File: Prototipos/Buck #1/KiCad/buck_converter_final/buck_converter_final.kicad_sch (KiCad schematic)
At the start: 31 parts, among them J2 Screw_Terminal_01x02, J3 Screw_Terminal_01x02, K1 SANYOU_SRD_Form_C, Q1 NPN, Q2 IRF9540NPBF, Q3 BC548

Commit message: PCB final, versión preliminar, con testpoints
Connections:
- net PWM_CONTROL: now also J1.15 (S7); no longer J1.9 (S1)
- net RETRO_MICRO: now also J1.17 (S9); no longer J1.11 (S3)
- net UC_RELAY: now also J1.16 (S8); no longer J1.10 (S2)
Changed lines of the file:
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@@
-	(wire
-		(pts
-			(xy 35.56 57.15) (xy 38.1 57.15)
-		)
-		(stroke
-			(width 0)
-			(type default)
-		)
-	)
 	(wire
 		(pts
@@
 	(wire
 		(pts
+			(xy 68.58 52.07) (xy 71.12 52.07)
+		)
+		(stroke
+			(width 0)
+			(type default)
+		)
+	)
+	(wire
+		(pts
 			(xy 259.08 93.98) (xy 261.62 93.98)
 		)
@@
 	(wire
 		(pts
-			(xy 35.56 54.61) (xy 38.1 54.61)
-		)
-		(stroke
-			(width 0)
-			(type default)
-		)
-	)
-	(wire
-		(pts
 			(xy 158.75 101.6) (xy 166.37 101.6)
 		)
@@
 	(wire
 		(pts
-			(xy 35.56 52.07) (xy 38.1 52.07)
-		)
-		(stroke
-			(width 0)
-			(type default)
-		)
-	)
-	(wire
-		(pts
 			(xy 158.75 97.79) (xy 158.75 101.6)
 		)
@@
 	(wire
 		(pts
+			(xy 35.56 69.85) (xy 38.1 69.85)
+		)
+		(stroke
+			(width 0)
+			(type default)
+		)
+	)
+	(wire
+		(pts
 			(xy 58.42 87.63) (xy 58.42 83.82)
 		)
@@
 		(pts
 			(xy 210.82 91.44) (xy 210.82 96.52)
+		)
+		(stroke
+			(width 0)
+			(type default)
+		)
+	)
+	(wire
+		(pts
+			(xy 35.56 67.31) (xy 38.1 67.31)
 		)
 		(stroke
@@
 	(global_label "RETRO_MICRO"
 		(shape input)
-		(at 35.56 57.15 180)
-		(fields_autoplaced yes)
-		(effects
-			(font
-				(size 1.27 1.27)
-			)
-			(justify right)
-		)
-		(property "Intersheetrefs" "${INTERSHEET_REFS}"
-			(at 19.6934 57.15 0)
-			(effects
-				(font
-					(size 1.27 1.27)
-				)
-				(justify right)
+		(at 71.12 52.07 0)
+		(fields_autoplaced yes)
+		(effects
+			(font
+				(size 1.27 1.27)
+			)
+			(justify left)
+		)
+		(property "Intersheetrefs" "${INTERSHEET_REFS}"
+			(at 86.9866 52.07 0)
+			(effects
+				(font
+					(size 1.27 1.27)
+				)
+				(justify left)
 				(hide yes)
 			)
@@
 	(global_label "PWM_CONTROL"
 		(shape output)
-		(at 35.56 52.07 180)
-		(fields_autoplaced yes)
-		(effects
-			(font
-				(size 1.27 1.27)
-			)
-			(justify right)
-		)
-		(property "Intersheetrefs" "${INTERSHEET_REFS}"
-			(at 18.9072 52.07 0)
+		(at 35.56 67.31 180)
+		(fields_autoplaced yes)
+		(effects
+			(font
+				(size 1.27 1.27)
+			)
+			(justify right)
+		)
+		(property "Intersheetrefs" "${INTERSHEET_REFS}"
+			(at 18.9072 67.31 0)
 			(effects
 				(font
@@
 	(global_label "UC_RELAY"
 		(shape output)
-		(at 35.56 54.61 180)
-		(fields_autoplaced yes)
-		(effects
-			(font
-				(size 1.27 1.27)
-			)
-			(justify right)
-		)
-		(property "Intersheetrefs" "${INTERSHEET_REFS}"
-			(at 23.3824 54.61 0)
-			(effects
-				(font
+		(at 35.56 69.85 180)
+		(fields_autoplaced yes)
+		(effects
+			(font
+				(size 1.27 1.27)
+			)
+			(justify right)
+		)
+		(property "Intersheetrefs" "${INTERSHEET_REFS}"
+			(at 23.3824 69.85 0)
+			(effects
+				(font

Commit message: Avances PCB
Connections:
- no-connect marks 0 -> 1
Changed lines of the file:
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@@
 		(color 0 0 0 0)
+	)
+	(no_connect
+		(at 44.45 120.65)
 	)
 	(wire

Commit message: PCB Buck versión 1.0 finalizada
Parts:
- added TP1: DRAIN, TestPoint:TestPoint_Loop_D1.80mm_Drill1.0mm_Beaded, symbol Connector:TestPoint
- added TP2: GATE, TestPoint:TestPoint_Loop_D1.80mm_Drill1.0mm_Beaded, symbol Connector:TestPoint
- added TP3: LOAD_1, TestPoint:TestPoint_Loop_D1.80mm_Drill1.0mm_Beaded, symbol Connector:TestPoint
- added TP4: LOAD_2, TestPoint:TestPoint_Loop_D1.80mm_Drill1.0mm_Beaded, symbol Connector:TestPoint
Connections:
- net GATE: now also TP2.1
- net INDUCTIVE_LOAD: now also TP4.1
- net RESISTIVE_LOAD: now also TP3.1
- net at C3.2, D2.2 (A), D3.1 (K)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: now also TP1.1
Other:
- moved on the sheet: J3

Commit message: Corrección footprint diodo
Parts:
- D3: footprint Diode_THT:D_DO-15_P12.70mm_Horizontal -> Diode_THT:D_DO-201AD_P12.70mm_Horizontal
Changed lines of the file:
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@@
 			)
 		)
-		(property "Footprint" "Diode_THT:D_DO-15_P12.70mm_Horizontal"
+		(property "Footprint" "Diode_THT:D_DO-201AD_P12.70mm_Horizontal"
 			(at 147.32 63.5 90)
 			(effects

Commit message: Corrección nomenclatura, lista de componentes
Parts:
- R10: value 2k2 -> 2.2k
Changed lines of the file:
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@@
 			)
 		)
-		(property "Value" "2k2"
+		(property "Value" "2.2k"
 			(at 172.466 64.516 0)
 			(effects

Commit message: Avances en medición de corriente
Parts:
- added C7, C8: 0.1uF, Capacitor_SMD:C_0805_2012Metric_Pad1.18x1.45mm_HandSolder, symbol Device:C_Small
- added R14, R15: 0.01, Resistor_SMD:R_0805_2012Metric_Pad1.20x1.40mm_HandSolder, symbol Device:R_Small
- added TP5: INDUCOR_CURRENT, TestPoint:TestPoint_Loop_D1.80mm_Drill1.0mm_Beaded, symbol Connector:TestPoint
- added TP6: CAPACITOR_CURRENT, TestPoint:TestPoint_Loop_D1.80mm_Drill1.0mm_Beaded, symbol Connector:TestPoint
- added U1, U2: INA199xxDCK, Package_TO_SOT_SMD:SOT-363_SC-70-6, symbol Amplifier_Current:INA199xxDCK
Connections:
- net 12V: now also C7.1, C8.1, U1.3 (V+), U2.3 (V+)
- net PGND: now also C7.2, R15.1, U1.1 (REF), U1.2 (GND), U2.5 (-); no longer C5.2
- net at C5.1, K1.1, R9.1: now also R14.2, U1.5 (-); no longer L1.2
- new net: TP5.1, U1.6
- new net: C8.2, U2.2 (GND)
- new net: C5.2, R15.2, U2.4 (+)
- new net: TP6.1, U2.6
- new net: L1.2, R14.1, U1.4 (+)
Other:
- moved on the sheet: C2, C5, C6, D1, D4, K1, L1, Q1, Q3, R1, R10, R11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

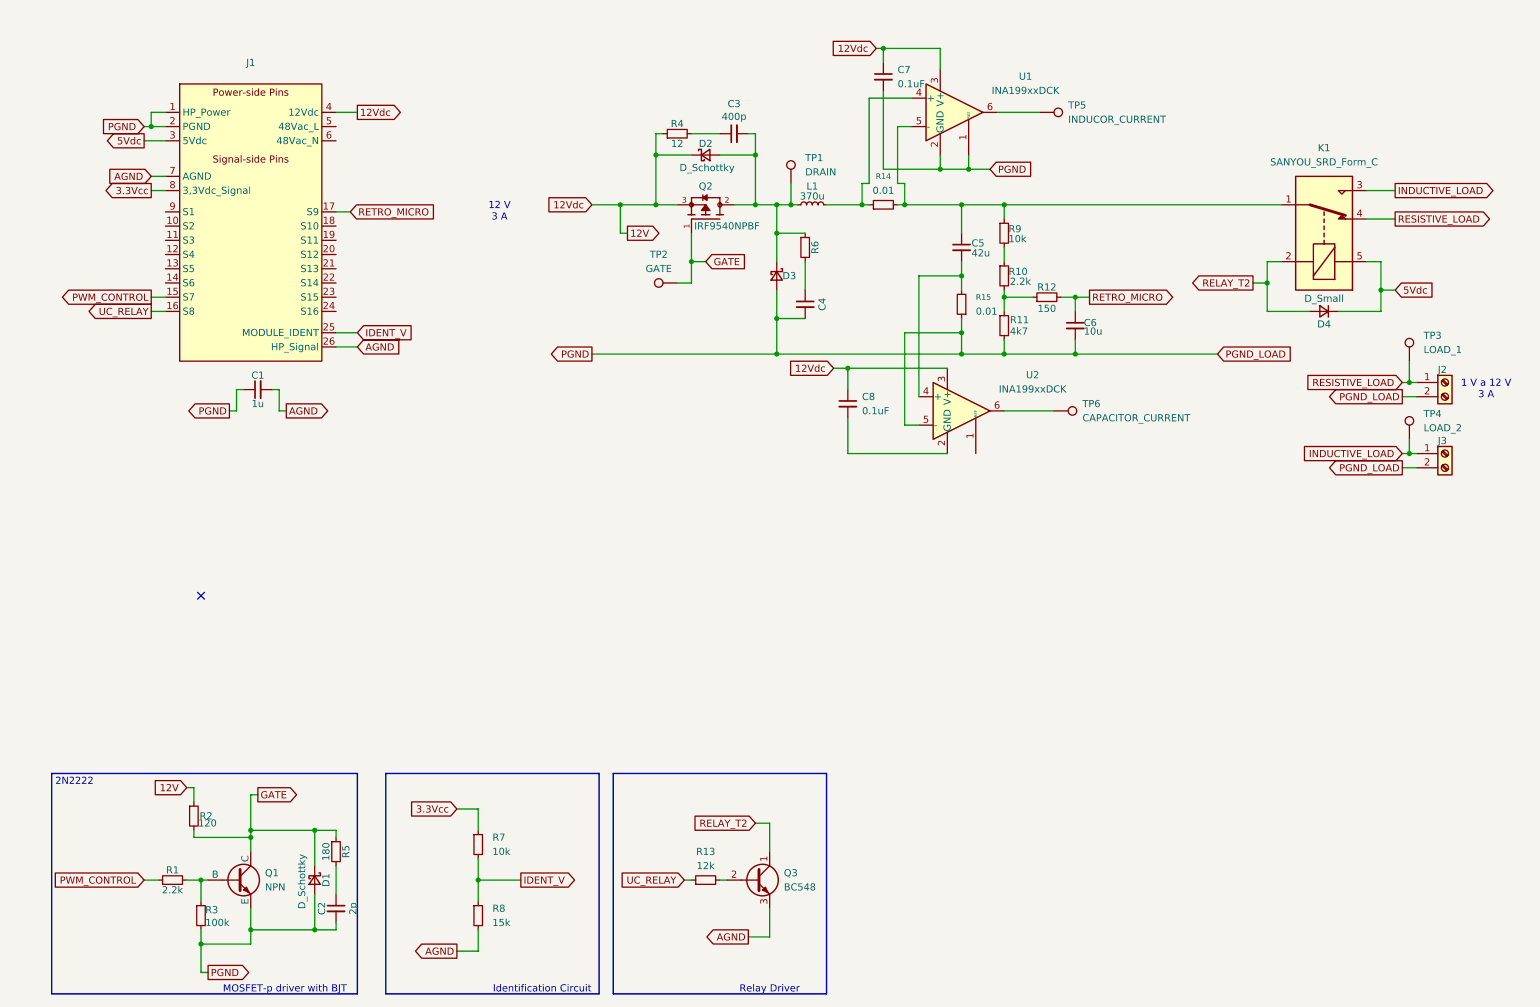
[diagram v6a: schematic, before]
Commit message: Agregado sensor corriente PCB
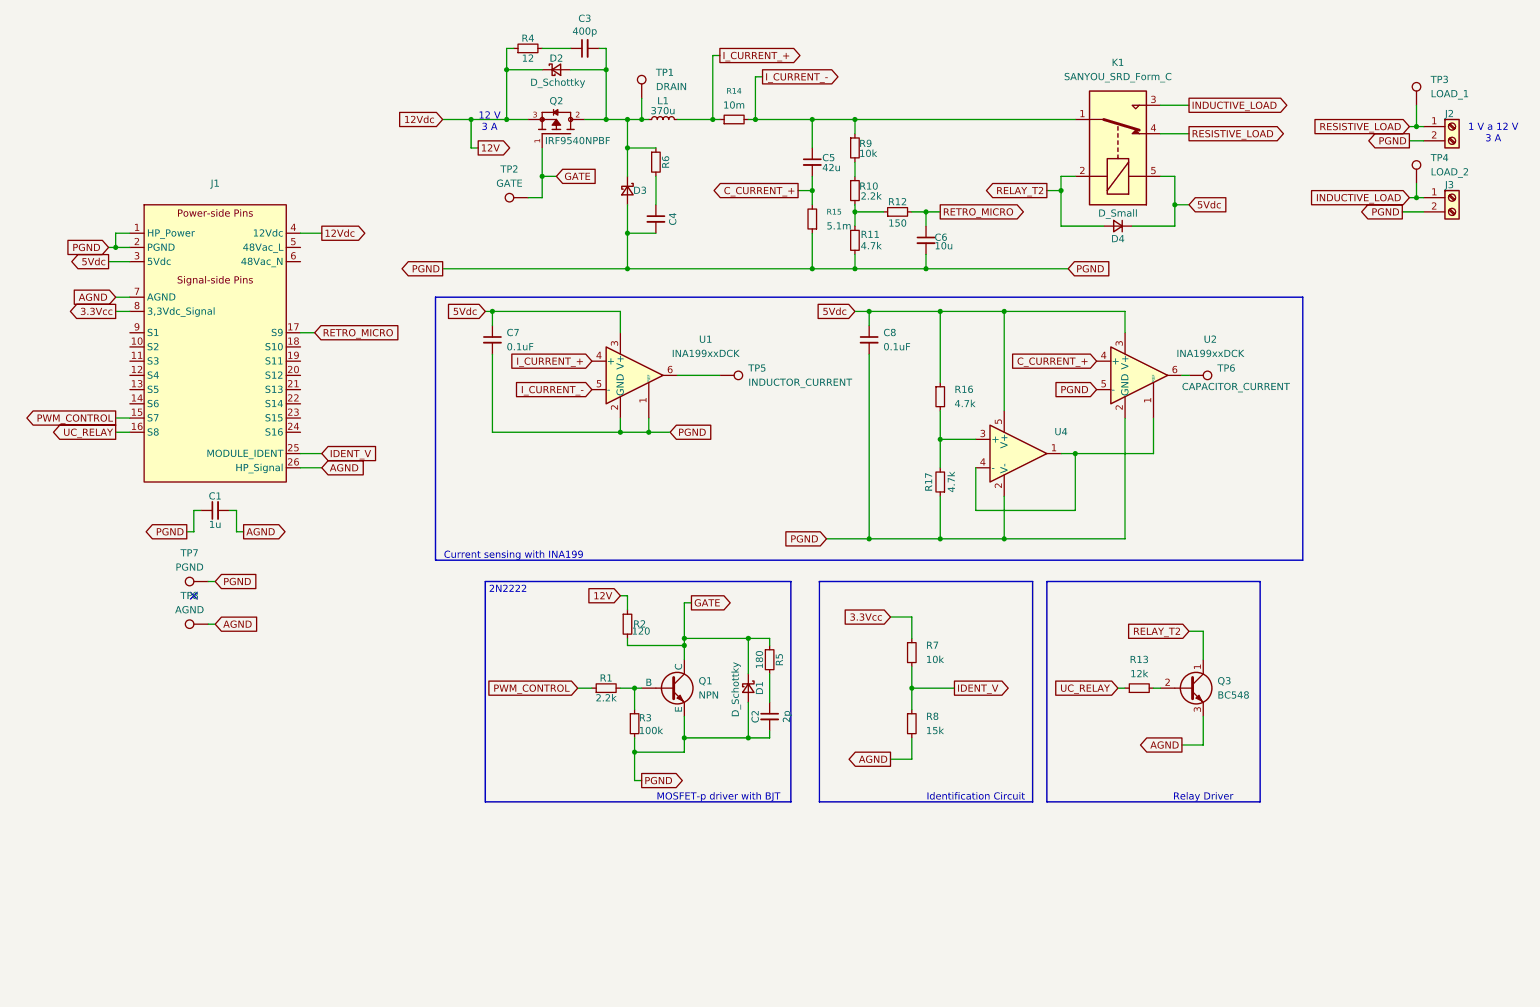
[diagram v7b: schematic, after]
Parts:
- added R16, R17: 4.7k, Resistor_SMD:R_0603_1608Metric_Pad0.98x0.95mm_HandSolder, symbol Device:R_Small
- added TP7: PGND, TestPoint:TestPoint_Loop_D1.80mm_Drill1.0mm_Beaded, symbol Connector:TestPoint
- added TP8: AGND, TestPoint:TestPoint_Loop_D1.80mm_Drill1.0mm_Beaded, symbol Connector:TestPoint
- added U4: TL071HIDBVR, TL071H:SOT23_DBV_5_TEX-M, symbol Simulation_SPICE:OPAMP
- R11: value 4k7 -> 4.7k
- R14: value 0.01 -> 10m
- R15: value 0.01 -> 5.1m
- TP5: value INDUCOR_CURRENT -> INDUCTOR_CURRENT
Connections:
- net 12V: no longer C7.1, C8.1, U1.3 (V+), U2.3 (V+)
- net 5Vdc: now also C7.1, C8.1, U1.3 (V+), U2.3 (V+), R16.1, U4.5 (V+)
- net AGND: now also TP8.1
- net PGND: now also C8.2, U2.2 (GND), R17.1, TP7.1, U4.2 (V-)
- net at U2.1 (REF): now also U4.1, U4.4 (-)
- net C_CURRENT_+: now reaches C5.2, R15.2, U2.4 (+)
- net I_CURRENT_-: now reaches C5.1, K1.1, R14.2, R9.1, U1.5 (-)
- net I_CURRENT_+: now reaches L1.2, R14.1, U1.4 (+)
- new net: R16.2, R17.2, U4.3 (+)
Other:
- note added: "Current sensing with INA199"
- moved on the sheet: C1, C2, C3, C4, C5, C6, C7, C8, D1, D2, D3, D4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

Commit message: PCB final
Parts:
- renumbered TP8 to REF_AGND1, TP7 to REF_PGND1
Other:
- moved on the sheet: REF_AGND1
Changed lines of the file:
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@@
 	(wire
 		(pts
-			(xy 45.72 125.73) (xy 46.99 125.73)
+			(xy 45.72 128.27) (xy 46.99 128.27)
 		)
 		(stroke
@@
 	(global_label "AGND"
 		(shape input)
-		(at 46.99 125.73 0)
+		(at 46.99 128.27 0)
 		(fields_autoplaced yes)
 		(effects
@@
 		)
 		(property "Intersheetrefs" "${INTERSHEET_REFS}"
-			(at 54.9343 125.73 0)
+			(at 54.9343 128.27 0)
 			(effects
 				(font
@@
 	(symbol
 		(lib_id "Connector:TestPoint")
-		(at 45.72 125.73 90)
+		(at 45.72 128.27 90)
 		(unit 1)
 		(exclude_from_sim no)
@@
 		(dnp no)
 		(fields_autoplaced yes)
-		(property "Reference" "TP8"
-			(at 42.418 120.65 90)
+		(property "Reference" "REF_AGND1"
+			(at 42.418 123.19 90)
 			(effects
 				(font
@@
 		)
 		(property "Value" "AGND"
-			(at 42.418 123.19 90)
+			(at 42.418 125.73 90)
 			(effects
 				(font
@@
 		)
 		(property "Footprint" "TestPoint:TestPoint_Loop_D1.80mm_Drill1.0mm_Beaded"
-			(at 45.72 120.65 0)
+			(at 45.72 123.19 0)
 			(effects
 				(font
@@
 		)
 		(property "Datasheet" "~"
-			(at 45.72 120.65 0)
+			(at 45.72 123.19 0)
 			(effects
 				(font
@@
 		)
 		(property "Description" "test point"
-			(at 45.72 125.73 0)
+			(at 45.72 128.27 0)
 			(effects
 				(font
@@
 			(project "buck_converter_final"
 				(path "/e3650d37-577f-4fda-9d2e-25068d42f977"
-					(reference "TP8")
+					(reference "REF_AGND1")
 					(unit 1)
 				)
@@
 		(dnp no)
 		(fields_autoplaced yes)
-		(property "Reference" "TP7"
+		(property "Reference" "REF_PGND1"
 			(at 42.418 113.03 90)
 			(effects
@@
 			(project "buck_converter_final"
 				(path "/e3650d37-577f-4fda-9d2e-25068d42f977"
-					(reference "TP7")
+					(reference "REF_PGND1")
 					(unit 1)
 				)
